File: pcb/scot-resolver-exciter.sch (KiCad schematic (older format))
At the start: 27 parts, among them IC1 AD8692ARMZ, IC2 AD8397ARZ

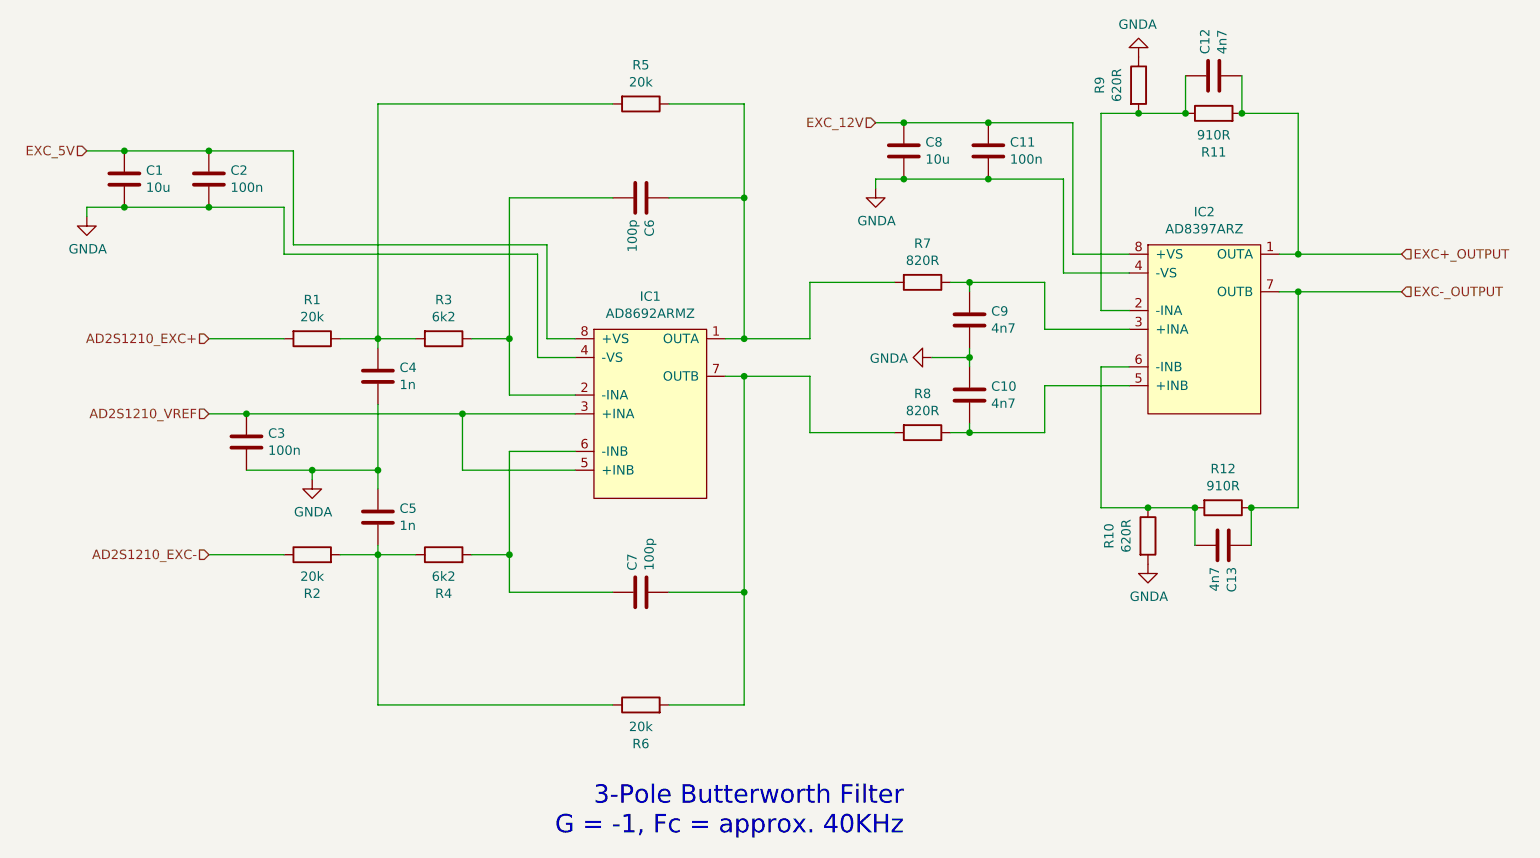
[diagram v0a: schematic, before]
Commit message: PCB Progress, laying tracks.
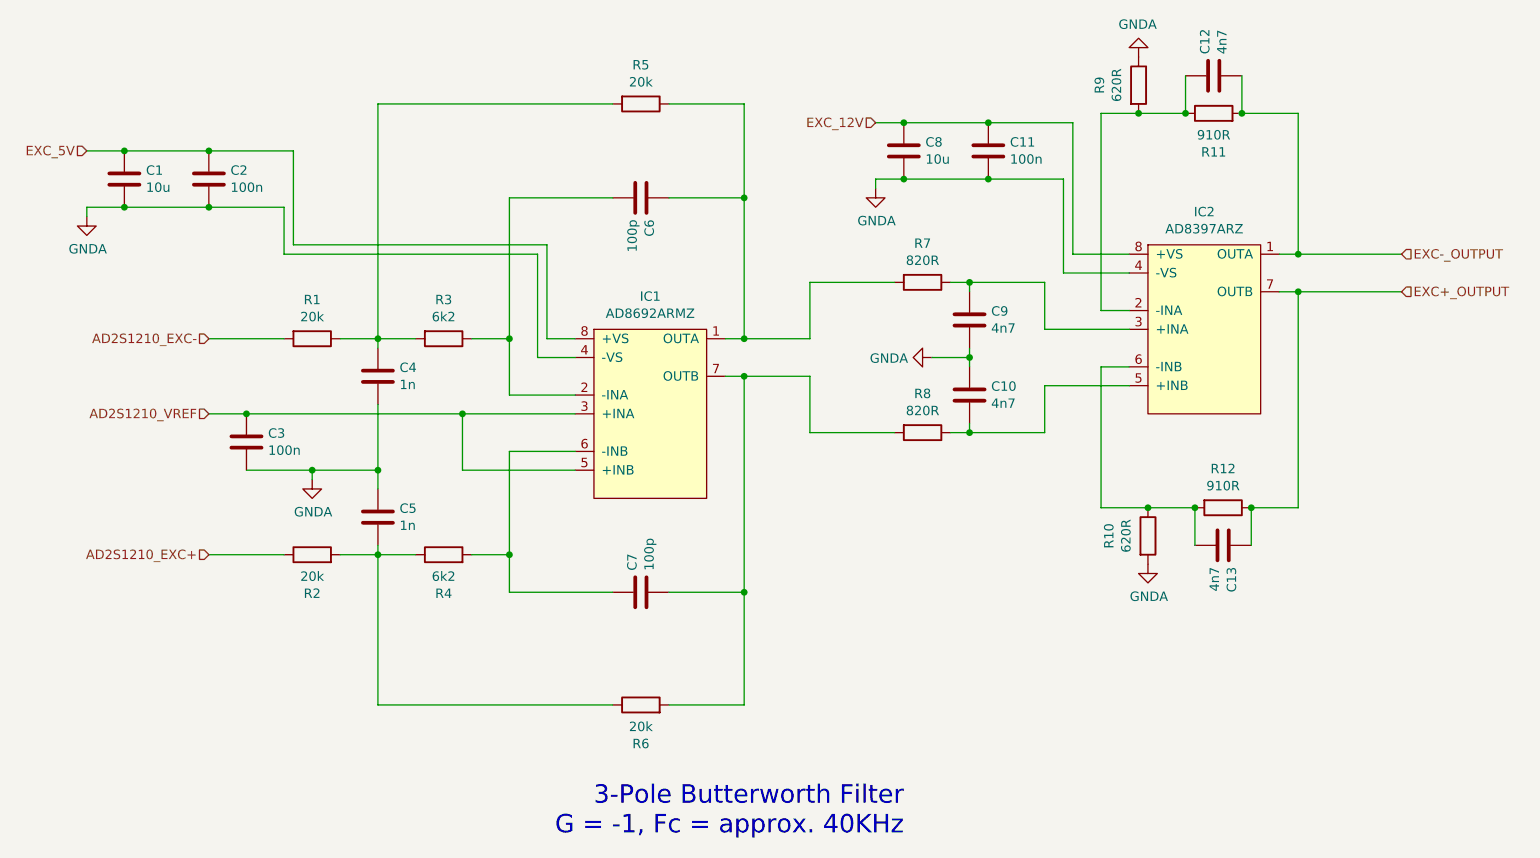
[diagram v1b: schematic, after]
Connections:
- net AD2S1210_EXC+: now also R2.1; no longer R1.2
- net AD2S1210_EXC-: now also R1.2; no longer R2.1
- net EXC+_OUTPUT: now also C13.1, IC2.7 (OUTB), R12.1; no longer C12.2, IC2.1 (OUTA), R11.2
- net EXC-_OUTPUT: now also C12.2, IC2.1 (OUTA), R11.2; no longer C13.1, IC2.7 (OUTB), R12.1
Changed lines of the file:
@@
 $EndComp
 Text HLabel 10050 2900 2    50   Input ~ 0
+EXC-_OUTPUT
+Text HLabel 10050 3100 2    50   Input ~ 0
 EXC+_OUTPUT
-Text HLabel 10050 3100 2    50   Input ~ 0
-EXC-_OUTPUT
 $Comp
 L Device:C C13
@@
 	3700 3750 3900 3750
 Text HLabel 3700 3350 0    50   Input ~ 0
+AD2S1210_EXC-
+Text HLabel 3700 4500 0    50   Input ~ 0
 AD2S1210_EXC+
-Text HLabel 3700 4500 0    50   Input ~ 0
-AD2S1210_EXC-
 Wire Wire Line
 	4100 4500 3700 4500

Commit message: pcb: V2 schematic updates (PCB still to do).
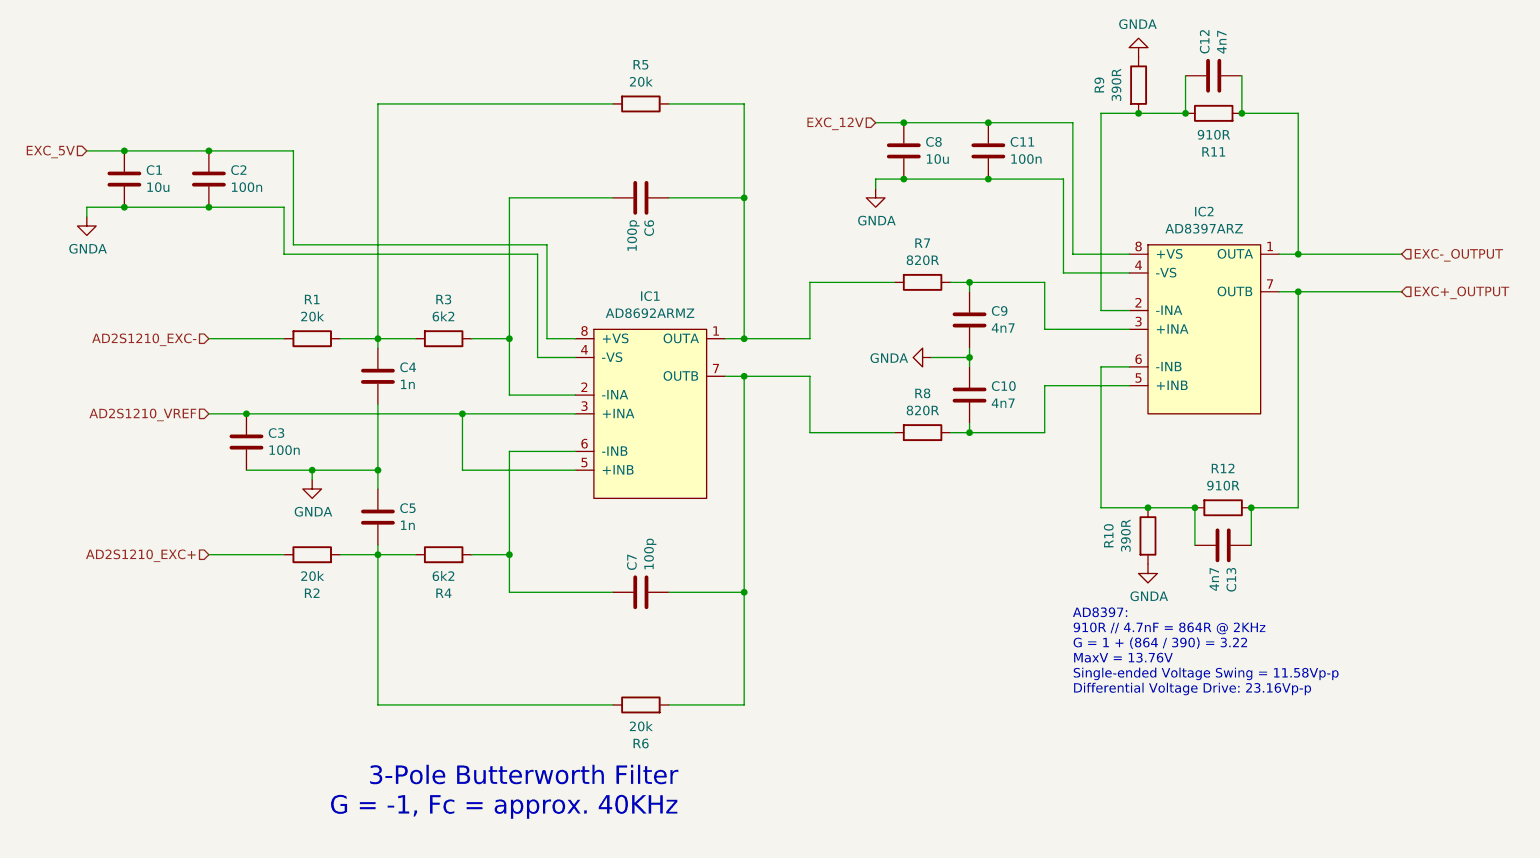
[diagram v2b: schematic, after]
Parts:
- R10, R9: value 620R -> 390R
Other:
- note added: "AD8397:\n910R // 4.7nF = 864R @ 2KHz\nG = 1 + (864 / 390) = 3.22\nMaxV = 13.76V\nSingle-ended Voltage Swing = 11.58Vp-p\nDifferential Voltage Drive: 23.16Vp-p"

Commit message: pcb: Add 10u to VREF, all 0402->0603
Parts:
- C10, C12, C13, C2, C3, C4, C5, C6, C7, C9: footprint Capacitor_SMD:C_0402_1005Metric -> Capacitor_SMD:C_0603_1608Metric_Pad1.05x0.95mm_HandSolder
- R1, R10, R11, R12, R2, R3, R4, R5, R6, R7, R8, R9: footprint Resistor_SMD:R_0402_1005Metric -> Resistor_SMD:R_0603_1608Metric_Pad1.05x0.95mm_HandSolder
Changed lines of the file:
@@
 F 0 "R2" V 4043 4500 50  0000 C CNN
 F 1 "20k" V 4134 4500 50  0000 C CNN
-F 2 "Resistor_SMD:R_0402_1005Metric" V 4180 4500 50  0001 C CNN
+F 2 "Resistor_SMD:R_0603_1608Metric_Pad1.05x0.95mm_HandSolder" V 4180 4500 50  0001 C CNN
 F 3 "~" H 4250 4500 50  0001 C CNN
 	1    4250 4500
@@
 F 0 "C4" H 4715 3596 50  0000 L CNN
 F 1 "1n" H 4715 3505 50  0000 L CNN
-F 2 "Capacitor_SMD:C_0402_1005Metric" H 4638 3400 50  0001 C CNN
+F 2 "Capacitor_SMD:C_0603_1608Metric_Pad1.05x0.95mm_HandSolder" H 4638 3400 50  0001 C CNN
 F 3 "~" H 4600 3550 50  0001 C CNN
 	1    4600 3550
@@
 F 0 "C6" H 6115 2646 50  0000 L CNN
 F 1 "100p" H 6115 2555 50  0000 L CNN
-F 2 "Capacitor_SMD:C_0402_1005Metric" H 6038 2450 50  0001 C CNN
+F 2 "Capacitor_SMD:C_0603_1608Metric_Pad1.05x0.95mm_HandSolder" H 6038 2450 50  0001 C CNN
 F 3 "~" H 6000 2600 50  0001 C CNN
 	1    6000 2600
@@
 F 0 "R8" V 7293 3850 50  0000 C CNN
 F 1 "820R" V 7384 3850 50  0000 C CNN
-F 2 "Resistor_SMD:R_0402_1005Metric" V 7430 3850 50  0001 C CNN
+F 2 "Resistor_SMD:R_0603_1608Metric_Pad1.05x0.95mm_HandSolder" V 7430 3850 50  0001 C CNN
 F 3 "~" H 7500 3850 50  0001 C CNN
 	1    7500 3850
@@
 F 0 "R11" V 8843 2150 50  0000 C CNN
 F 1 "910R" V 8934 2150 50  0000 C CNN
-F 2 "Resistor_SMD:R_0402_1005Metric" V 8980 2150 50  0001 C CNN
+F 2 "Resistor_SMD:R_0603_1608Metric_Pad1.05x0.95mm_HandSolder" V 8980 2150 50  0001 C CNN
 F 3 "~" H 9050 2150 50  0001 C CNN
 	1    9050 2150
@@
 F 0 "R9" V 8443 2000 50  0000 C CNN
 F 1 "390R" V 8534 2000 50  0000 C CNN
-F 2 "Resistor_SMD:R_0402_1005Metric" V 8580 2000 50  0001 C CNN
+F 2 "Resistor_SMD:R_0603_1608Metric_Pad1.05x0.95mm_HandSolder" V 8580 2000 50  0001 C CNN
 F 3 "~" H 8650 2000 50  0001 C CNN
 	1    8650 2000
@@
 F 0 "C13" H 9215 4496 50  0000 L CNN
 F 1 "4n7" H 9215 4405 50  0000 L CNN
-F 2 "Capacitor_SMD:C_0402_1005Metric" H 9138 4300 50  0001 C CNN
+F 2 "Capacitor_SMD:C_0603_1608Metric_Pad1.05x0.95mm_HandSolder" H 9138 4300 50  0001 C CNN
 F 3 "~" H 9100 4450 50  0001 C CNN
 	1    9100 4450
@@
 F 0 "R12" V 8893 4250 50  0000 C CNN
 F 1 "910R" V 8984 4250 50  0000 C CNN
-F 2 "Resistor_SMD:R_0402_1005Metric" V 9030 4250 50  0001 C CNN
+F 2 "Resistor_SMD:R_0603_1608Metric_Pad1.05x0.95mm_HandSolder" V 9030 4250 50  0001 C CNN
 F 3 "~" H 9100 4250 50  0001 C CNN
 	1    9100 4250
@@
 F 0 "R10" V 8493 4400 50  0000 C CNN
 F 1 "390R" V 8584 4400 50  0000 C CNN
-F 2 "Resistor_SMD:R_0402_1005Metric" V 8630 4400 50  0001 C CNN
+F 2 "Resistor_SMD:R_0603_1608Metric_Pad1.05x0.95mm_HandSolder" V 8630 4400 50  0001 C CNN
 F 3 "~" H 8700 4400 50  0001 C CNN
 	1    8700 4400
@@
 F 0 "C10" H 7865 3696 50  0000 L CNN
 F 1 "4n7" H 7865 3605 50  0000 L CNN
-F 2 "Capacitor_SMD:C_0402_1005Metric" H 7788 3500 50  0001 C CNN
+F 2 "Capacitor_SMD:C_0603_1608Metric_Pad1.05x0.95mm_HandSolder" H 7788 3500 50  0001 C CNN
 F 3 "~" H 7750 3650 50  0001 C CNN
 	1    7750 3650
@@
 F 0 "C9" H 7865 3296 50  0000 L CNN
 F 1 "4n7" H 7865 3205 50  0000 L CNN
-F 2 "Capacitor_SMD:C_0402_1005Metric" H 7788 3100 50  0001 C CNN
+F 2 "Capacitor_SMD:C_0603_1608Metric_Pad1.05x0.95mm_HandSolder" H 7788 3100 50  0001 C CNN
 F 3 "~" H 7750 3250 50  0001 C CNN
 	1    7750 3250
@@
 F 0 "R7" V 7293 3050 50  0000 C CNN
 F 1 "820R" V 7384 3050 50  0000 C CNN
-F 2 "Resistor_SMD:R_0402_1005Metric" V 7430 3050 50  0001 C CNN
+F 2 "Resistor_SMD:R_0603_1608Metric_Pad1.05x0.95mm_HandSolder" V 7430 3050 50  0001 C CNN
 F 3 "~" H 7500 3050 50  0001 C CNN
 	1    7500 3050
@@
 F 0 "C7" H 6115 4746 50  0000 L CNN
 F 1 "100p" H 6115 4655 50  0000 L CNN
-F 2 "Capacitor_SMD:C_0402_1005Metric" H 6038 4550 50  0001 C CNN
+F 2 "Capacitor_SMD:C_0603_1608Metric_Pad1.05x0.95mm_HandSolder" H 6038 4550 50  0001 C CNN
 F 3 "~" H 6000 4700 50  0001 C CNN
 	1    6000 4700
@@
 F 0 "R4" V 4743 4500 50  0000 C CNN
 F 1 "6k2" V 4834 4500 50  0000 C CNN
-F 2 "Resistor_SMD:R_0402_1005Metric" V 4880 4500 50  0001 C CNN
+F 2 "Resistor_SMD:R_0603_1608Metric_Pad1.05x0.95mm_HandSolder" V 4880 4500 50  0001 C CNN
 F 3 "~" H 4950 4500 50  0001 C CNN
 	1    4950 4500
@@
 F 0 "C5" H 4715 4346 50  0000 L CNN
 F 1 "1n" H 4715 4255 50  0000 L CNN
-F 2 "Capacitor_SMD:C_0402_1005Metric" H 4638 4150 50  0001 C CNN
+F 2 "Capacitor_SMD:C_0603_1608Metric_Pad1.05x0.95mm_HandSolder" H 4638 4150 50  0001 C CNN
 F 3 "~" H 4600 4300 50  0001 C CNN
 	1    4600 4300
@@
 F 0 "R1" V 4043 3350 50  0000 C CNN
 F 1 "20k" V 4134 3350 50  0000 C CNN
-F 2 "Resistor_SMD:R_0402_1005Metric" V 4180 3350 50  0001 C CNN
+F 2 "Resistor_SMD:R_0603_1608Metric_Pad1.05x0.95mm_HandSolder" V 4180 3350 50  0001 C CNN
 F 3 "~" H 4250 3350 50  0001 C CNN
 	1    4250 3350
@@
 F 0 "R5" V 5793 2100 50  0000 C CNN
 F 1 "20k" V 5884 2100 50  0000 C CNN
-F 2 "Resistor_SMD:R_0402_1005Metric" V 5930 2100 50  0001 C CNN
+F 2 "Resistor_SMD:R_0603_1608Metric_Pad1.05x0.95mm_HandSolder" V 5930 2100 50  0001 C CNN
 F 3 "~" H 6000 2100 50  0001 C CNN
 	1    6000 2100
@@
 F 0 "R6" V 5793 5300 50  0000 C CNN
 F 1 "20k" V 5884 5300 50  0000 C CNN
-F 2 "Resistor_SMD:R_0402_1005Metric" V 5930 5300 50  0001 C CNN
+F 2 "Resistor_SMD:R_0603_1608Metric_Pad1.05x0.95mm_HandSolder" V 5930 5300 50  0001 C CNN
 F 3 "~" H 6000 5300 50  0001 C CNN
 	1    6000 5300
@@
 F 0 "R3" V 4743 3350 50  0000 C CNN
 F 1 "6k2" V 4834 3350 50  0000 C CNN
-F 2 "Resistor_SMD:R_0402_1005Metric" V 4880 3350 50  0001 C CNN
+F 2 "Resistor_SMD:R_0603_1608Metric_Pad1.05x0.95mm_HandSolder" V 4880 3350 50  0001 C CNN
 F 3 "~" H 4950 3350 50  0001 C CNN
 	1    4950 3350
@@
 F 0 "C3" H 4015 3946 50  0000 L CNN
 F 1 "100n" H 4015 3855 50  0000 L CNN
-F 2 "Capacitor_SMD:C_0402_1005Metric" H 3938 3750 50  0001 C CNN
+F 2 "Capacitor_SMD:C_0603_1608Metric_Pad1.05x0.95mm_HandSolder" H 3938 3750 50  0001 C CNN
 F 3 "~" H 3900 3900 50  0001 C CNN
 	1    3900 3900
@@
 F 0 "C2" H 3815 2546 50  0000 L CNN
 F 1 "100n" H 3815 2455 50  0000 L CNN
-F 2 "Capacitor_SMD:C_0402_1005Metric" H 3738 2350 50  0001 C CNN
+F 2 "Capacitor_SMD:C_0603_1608Metric_Pad1.05x0.95mm_HandSolder" H 3738 2350 50  0001 C CNN
 F 3 "~" H 3700 2500 50  0001 C CNN
 	1    3700 2500
@@
 F 0 "C12" H 9165 1996 50  0000 L CNN
 F 1 "4n7" H 9165 1905 50  0000 L CNN
-F 2 "Capacitor_SMD:C_0402_1005Metric" H 9088 1800 50  0001 C CNN
+F 2 "Capacitor_SMD:C_0603_1608Metric_Pad1.05x0.95mm_HandSolder" H 9088 1800 50  0001 C CNN
 F 3 "~" H 9050 1950 50  0001 C CNN
 	1    9050 1950
